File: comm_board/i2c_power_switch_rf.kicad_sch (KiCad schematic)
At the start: 7 parts, among them U4 MCP23008T-E/SS, U5 INA226AIDGSR

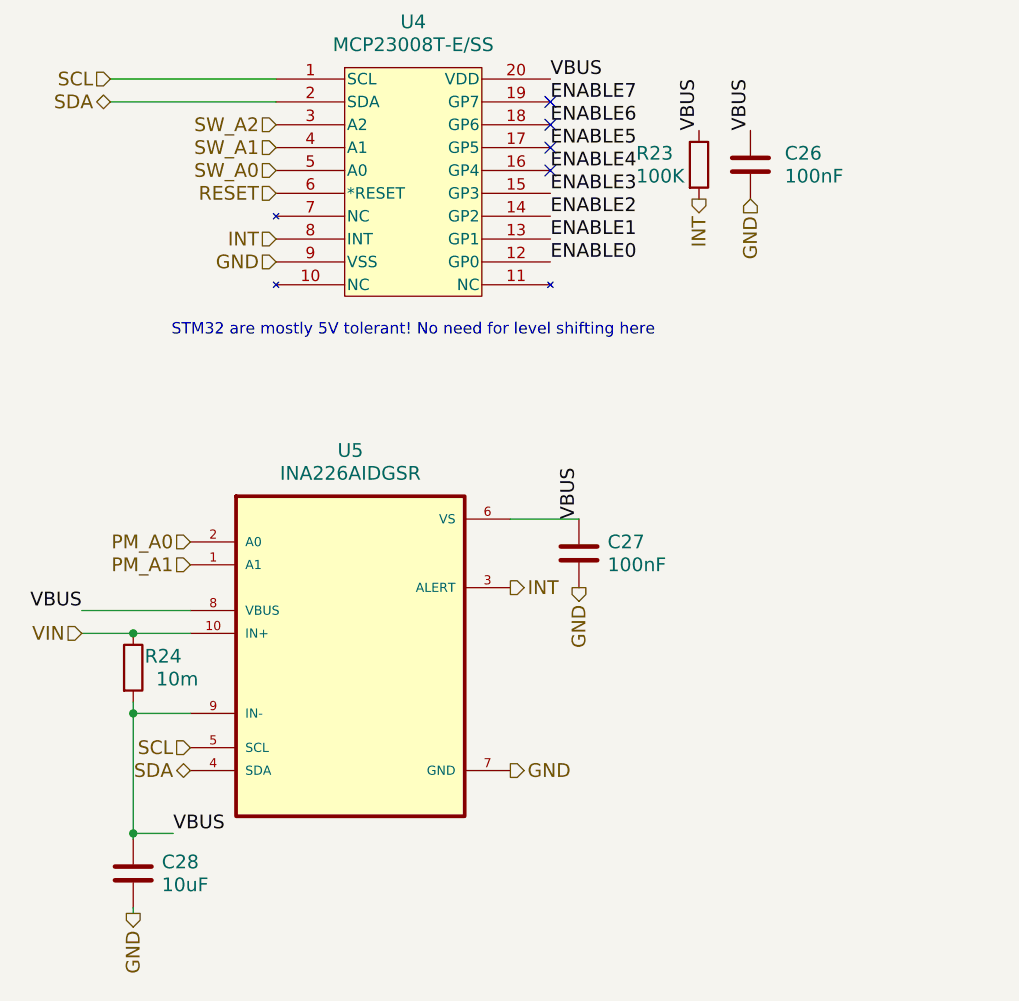
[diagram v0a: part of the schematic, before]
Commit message: moving common sheets to common, cleanup for some missed files
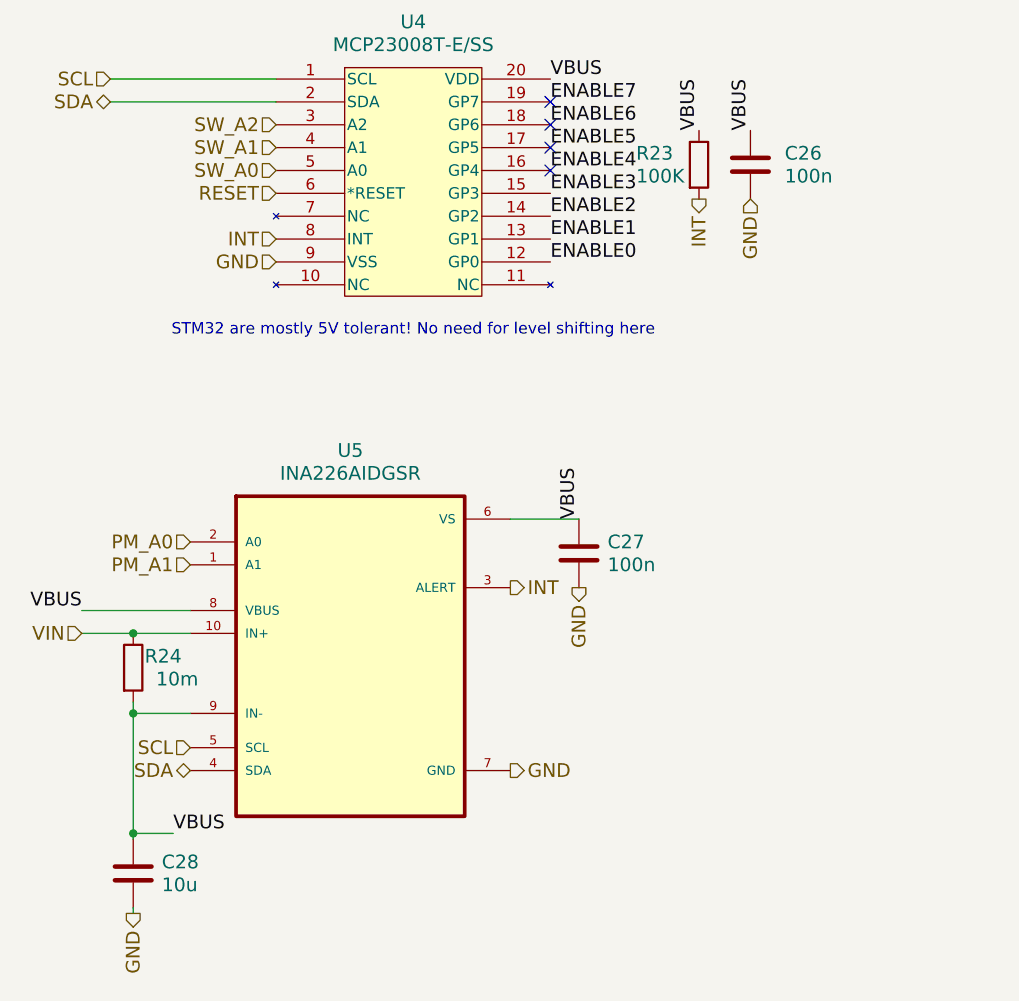
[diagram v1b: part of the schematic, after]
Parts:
- C26, C27: value 100nF -> 100n
- C28: value 10uF -> 10u
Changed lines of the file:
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@@
 			)
 		)
-		(property "Value" "10uF"
+		(property "Value" "10u"
 			(at 52.07 121.2849 0)
 			(effects
@@
 			)
 		)
-		(property "Value" "100nF"
+		(property "Value" "100n"
 			(at 121.285 42.5449 0)
 			(effects
@@
 			)
 		)
-		(property "Value" "100nF"
+		(property "Value" "100n"
 			(at 101.6 85.7249 0)
 			(effects
